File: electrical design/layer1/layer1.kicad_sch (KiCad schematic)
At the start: 183 parts, among them J1 XT60-F, J2 1x07 2.54 FEMALE, J3 1x07 2.54 FEMALE, Q1 MOSFET-NCH-FQP30N06L, Q2 MOSFET-NCH-AO3404A, SW1 SW_DPDT_x2, U1 CD74HC4067SM, U2 CD74HC4067SM

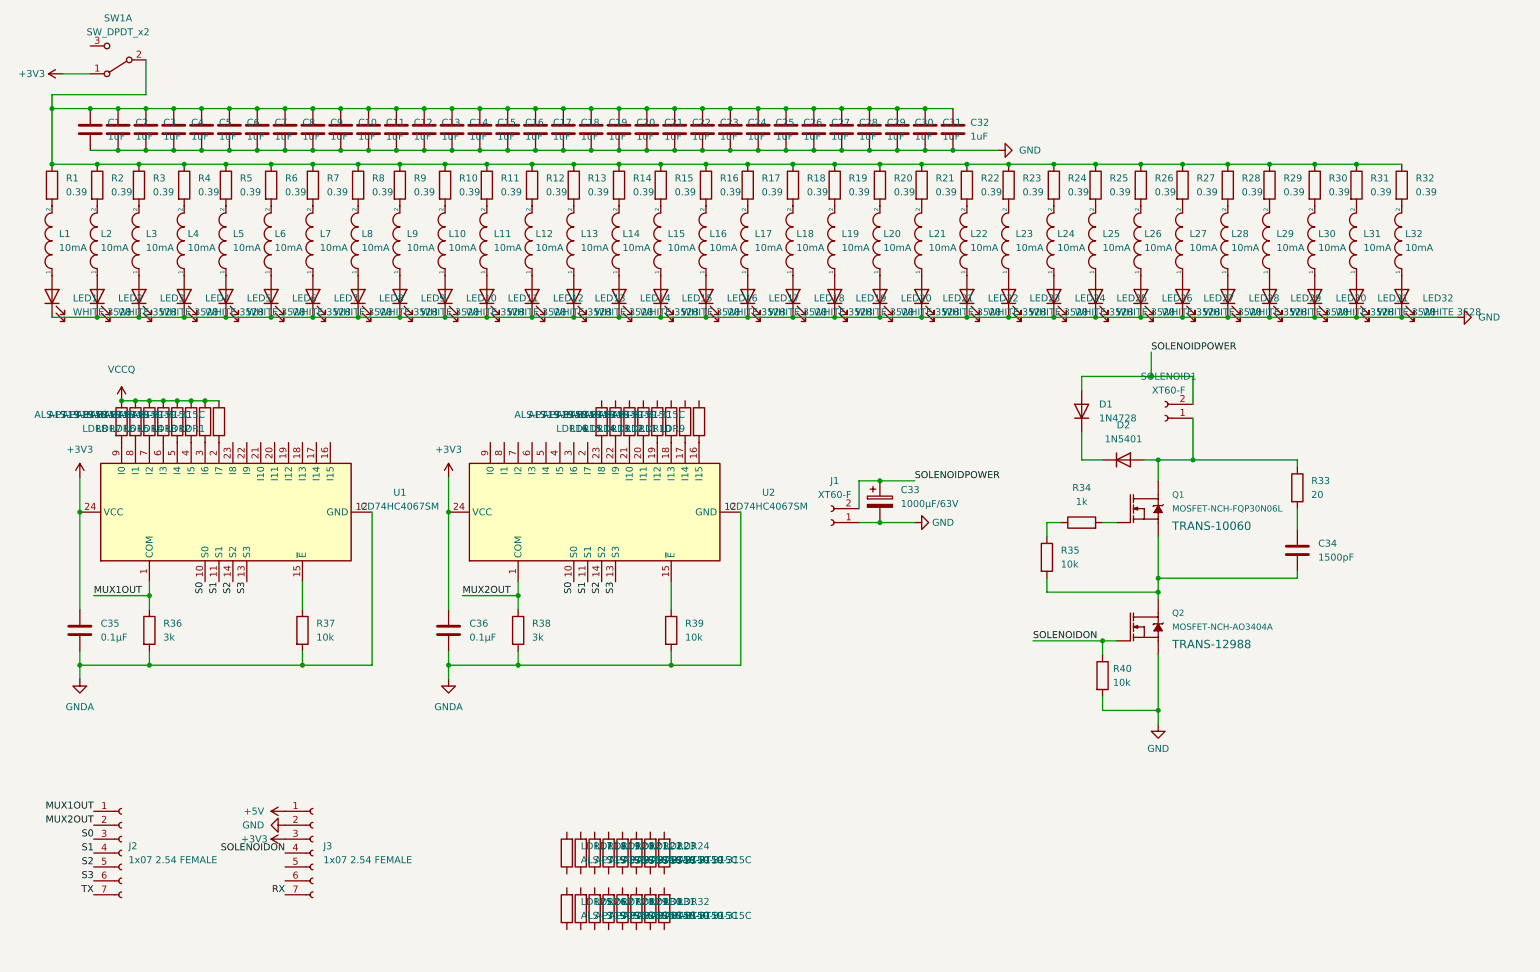
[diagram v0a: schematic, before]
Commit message: update layer 1 pcb
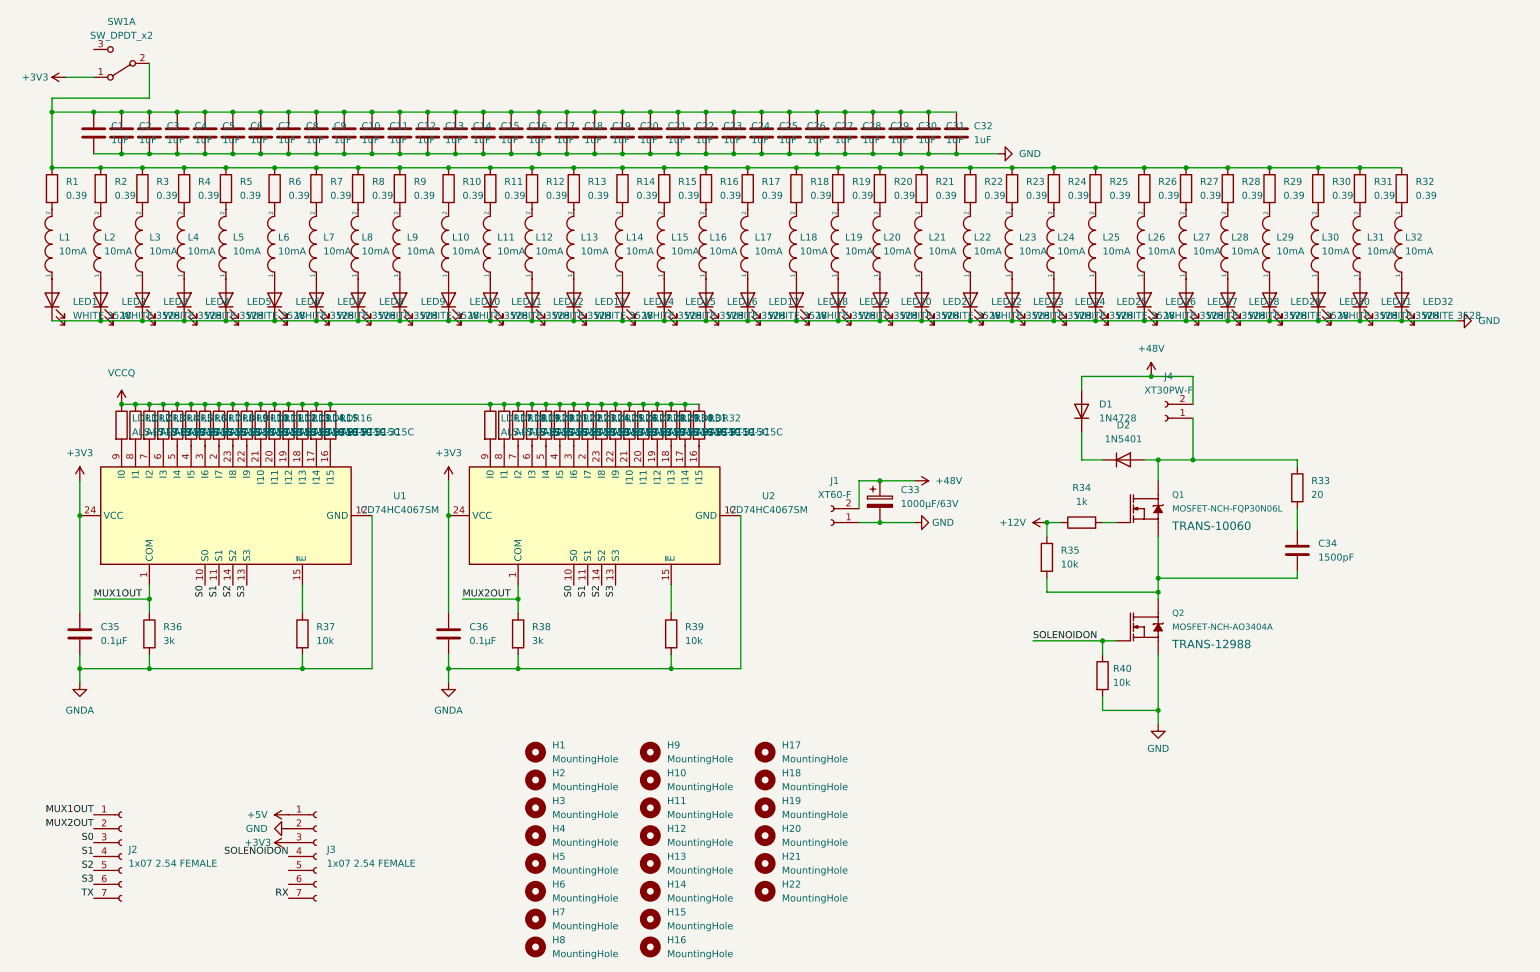
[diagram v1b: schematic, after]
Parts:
- added H1, H10, H11, H12, H13, H14, H15, H16, H17, H18, H19, H2, H20, H21, H22, H3, H4, H5, H6, H7, H8, H9: MountingHole, MountingHole:MountingHole_3.2mm_M3_Pad, symbol Mechanical:MountingHole
- J4: renamed from SOLENOID1; value XT60-F -> XT30PW-F; footprint Connector_AMASS:AMASS_XT30UPB-F_1x02_P5.0mm_Vertical -> Connector_AMASS:AMASS_XT30PW-F_1x02_P2.50mm_Horizontal
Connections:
- net VCCQ: now also LDR10.1, LDR11.1, LDR12.1, LDR13.1, LDR14.1, LDR15.1, LDR16.1, LDR17.1, LDR18.1, LDR19.1, LDR20.1, LDR21.1, LDR22.1, LDR23.1, LDR24.1, LDR25.1, LDR26.1, LDR27.1, LDR28.1, LDR29.1, LDR30.1, LDR31.1, LDR32.1, LDR9.1
- net at U1.16 (I15): now also LDR16.2
- net at U1.17 (I14): now also LDR15.2
- net at U1.18 (I13): now also LDR14.2
- net at U1.19 (I12): now also LDR13.2
- net at U1.2 (I7): now also LDR8.2; no longer LDR1.2
- net at U1.20 (I11): now also LDR12.2
- net at U1.21 (I10): now also LDR11.2
- net at U1.22 (I9): now also LDR10.2
- net at U1.23 (I8): now also LDR9.2
- net at U1.3 (I6): now also LDR7.2; no longer LDR2.2
- net at U1.4 (I5): now also LDR6.2; no longer LDR3.2
- net at U1.5 (I4): now also LDR5.2; no longer LDR4.2
- net at U1.6 (I3): now also LDR4.2; no longer LDR5.2
- net at U1.7 (I2): now also LDR3.2; no longer LDR6.2
- net at U1.8 (I1): now also LDR2.2; no longer LDR7.2
- net at U1.9 (I0): now also LDR1.2; no longer LDR8.2
- net +12V: now reaches R34.1, R35.1
- net at LDR28.2: now also U2.20 (I11)
- net at U2.16 (I15): now also LDR32.2; no longer LDR9.2
- net at U2.17 (I14): now also LDR31.2; no longer LDR10.2
- net at U2.18 (I13): now also LDR30.2; no longer LDR11.2
- net at U2.19 (I12): now also LDR29.2; no longer LDR12.2
- net at U2.2 (I7): now also LDR24.2
- net at U2.21 (I10): now also LDR27.2; no longer LDR14.2
- net at U2.22 (I9): now also LDR26.2; no longer LDR15.2
- net at U2.23 (I8): now also LDR25.2; no longer LDR16.2
- net at U2.3 (I6): now also LDR23.2
- net at U2.4 (I5): now also LDR22.2
- net at U2.5 (I4): now also LDR21.2
- net at U2.6 (I3): now also LDR20.2
- net at U2.7 (I2): now also LDR19.2
- net at U2.8 (I1): now also LDR18.2
- net at U2.9 (I0): now also LDR17.2
- net SOLENOIDPOWER renamed +48V
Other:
- company: (none) -> 8076ducc Robotics Competition Team
- title: (none) -> layer 1 schematic drawing
- moved on the sheet: C1, C10, C11, C12, C13, C14, C15, C16, C17, C18, C19, C2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

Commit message: add boost to l1 pcb and update mech drawing
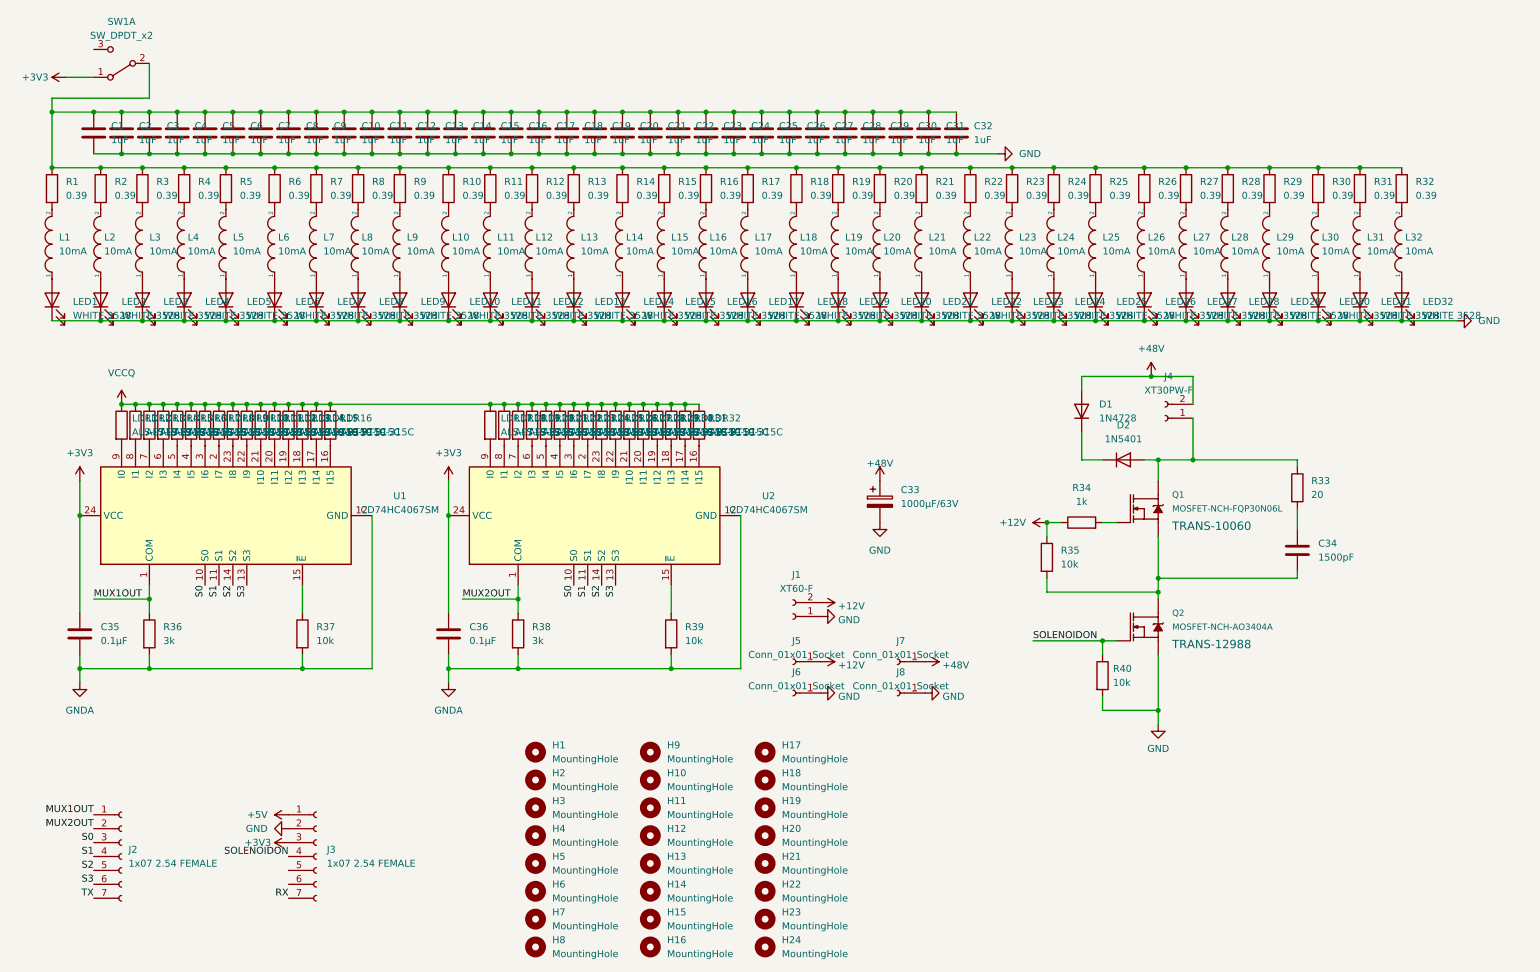
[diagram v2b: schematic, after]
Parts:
- added H23, H24: MountingHole, MountingHole:MountingHole_3.2mm_M3_Pad, symbol Mechanical:MountingHole
- added J5, J6, J7, J8: Conn_01x01_Socket, Connector_Wire:SolderWirePad_1x01_SMD_5x10mm, symbol Connector:Conn_01x01_Socket
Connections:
- net +12V: now also J1.2 (Pin_2), J5.1 (Pin_1)
- net +48V: now also J7.1 (Pin_1); no longer J1.2 (Pin_2)
- net GND: now also J6.1 (Pin_1), J8.1 (Pin_1)
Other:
- moved on the sheet: J1

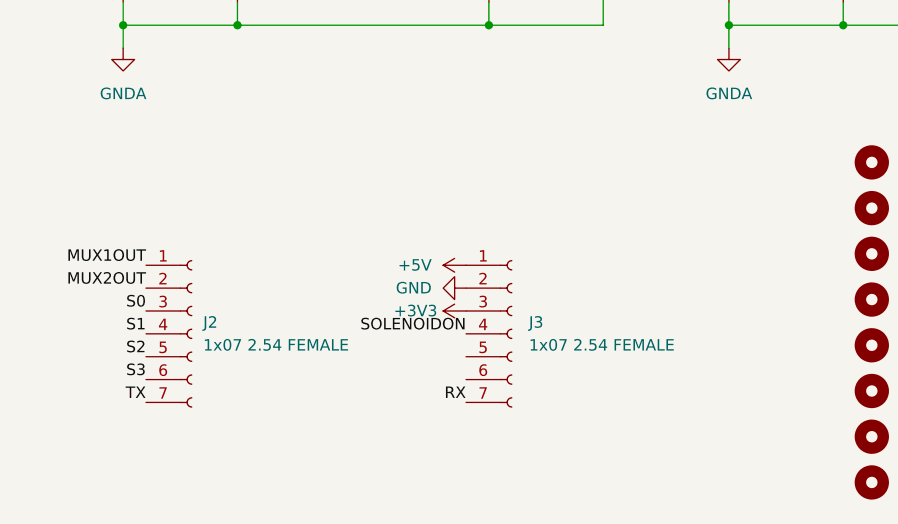
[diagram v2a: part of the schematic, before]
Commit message: route l1 signal lines and resolve drc issues
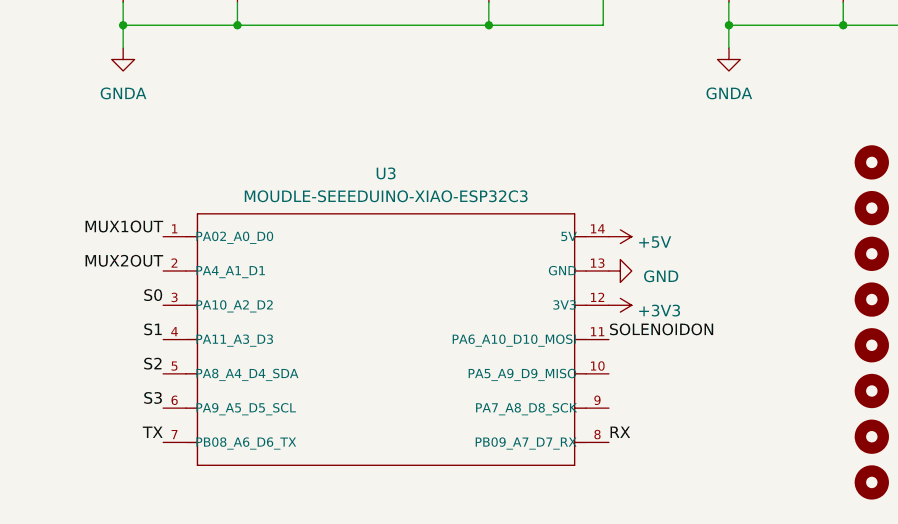
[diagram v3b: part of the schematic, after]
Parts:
- removed J2, J3: 1x07 2.54 FEMALE, Connector_PinHeader_2.54mm:PinHeader_1x07_P2.54mm_Vertical, symbol Connector:Conn_01x07_Female
- added U3: MOUDLE-SEEEDUINO-XIAO-ESP32C3, libraries:xiao-esp32c3, symbol MOUDLE-SEEEDUINO-XIAO-ESP32C3:MOUDLE-SEEEDUINO-XIAO-ESP32C3
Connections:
- net +3V3: now also U3.12 (3V3)
- net +5V: now also U3.14 (5V)
- net GND: now also U3.13 (GND)
- net MUX1OUT: now also U3.1 (PA02_A0_D0)
- net MUX2OUT: now also U3.2 (PA4_A1_D1)
- net RX: now also U3.8 (PB09_A7_D7_RX)
- net S0: now also U3.3 (PA10_A2_D2)
- net S1: now also U3.4 (PA11_A3_D3)
- net S2: now also U3.5 (PA8_A4_D4_SDA)
- net S3: now also U3.6 (PA9_A5_D5_SCL)
- net SOLENOIDON: now also U3.11 (PA6_A10_D10_MOSI)
- net TX: now also U3.7 (PB08_A6_D6_TX)
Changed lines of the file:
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@@
     (stroke (width 0) (type default))
   )
-  (label "MUX1OUT" (at 29.21 163.83 180) (fields_autoplaced)
+  (label "MUX1OUT" (at 31.115 160.655 180) (fields_autoplaced)
     (effects (font (size 1.27 1.27)) (justify right bottom))
   )
@@
     (effects (font (size 1.27 1.27)) (justify right bottom))
   )
-  (label "MUX2OUT" (at 29.21 166.37 180) (fields_autoplaced)
+  (label "MUX2OUT" (at 31.115 164.465 180) (fields_autoplaced)
     (effects (font (size 1.27 1.27)) (justify right bottom))
   )
-  (label "S3" (at 29.21 176.53 180) (fields_autoplaced)
+  (label "S3" (at 31.115 179.705 180) (fields_autoplaced)
     (effects (font (size 1.27 1.27)) (justify right bottom))
   )
-  (label "S0" (at 29.21 168.91 180) (fields_autoplaced)
+  (label "S0" (at 31.115 168.275 180) (fields_autoplaced)
     (effects (font (size 1.27 1.27)) (justify right bottom))
   )
@@
     (effects (font (size 1.27 1.27)) (justify right bottom))
   )
-  (label "RX" (at 64.77 179.07 180) (fields_autoplaced)
-    (effects (font (size 1.27 1.27)) (justify right bottom))
+  (label "RX" (at 80.645 183.515 0) (fields_autoplaced)
+    (effects (font (size 1.27 1.27)) (justify left bottom))
   )
   (label "MUX1OUT" (at 29.21 124.46 0) (fields_autoplaced)
     (effects (font (size 1.27 1.27)) (justify left bottom))
   )
-  (label "S2" (at 29.21 173.99 180) (fields_autoplaced)
+  (label "S2" (at 31.115 175.895 180) (fields_autoplaced)
     (effects (font (size 1.27 1.27)) (justify right bottom))
   )
@@
     (effects (font (size 1.27 1.27)) (justify right bottom))
   )
-  (label "S1" (at 29.21 171.45 180) (fields_autoplaced)
+  (label "S1" (at 31.115 172.085 180) (fields_autoplaced)
     (effects (font (size 1.27 1.27)) (justify right bottom))
   )
-  (label "TX" (at 29.21 179.07 180) (fields_autoplaced)
+  (label "TX" (at 31.115 183.515 180) (fields_autoplaced)
     (effects (font (size 1.27 1.27)) (justify right bottom))
   )
-  (label "SOLENOIDON" (at 64.77 171.45 180) (fields_autoplaced)
-    (effects (font (size 1.27 1.27)) (justify right bottom))
+  (label "SOLENOIDON" (at 80.645 172.085 0) (fields_autoplaced)
+    (effects (font (size 1.27 1.27)) (justify left bottom))
   )
   (label "S2" (at 121.92 121.92 270) (fields_autoplaced)
@@
     )
   )
-  (symbol (lib_id "power:GND") (at 64.77 166.37 270) (unit 1)
+  (symbol (lib_id "power:GND") (at 80.645 164.465 90) (unit 1)
     (in_bom yes) (on_board yes) (dnp no) (fields_autoplaced)
-    (property "Reference" "#PWR010" (at 58.42 166.37 0)
+    (property "Reference" "#PWR010" (at 86.995 164.465 0)
       (effects (font (size 1.27 1.27)) hide)
     )
-    (property "Value" "GND" (at 60.96 166.3699 90)
+    (property "Value" "GND" (at 84.455 165.1 90)
       (effects (font (size 1.27 1.27)) (justify right))
     )
-    (property "Footprint" "" (at 64.77 166.37 0)
+    (property "Footprint" "" (at 80.645 164.465 0)
       (effects (font (size 1.27 1.27)) hide)
     )
-    (property "Datasheet" "" (at 64.77 166.37 0)
+    (property "Datasheet" "" (at 80.645 164.465 0)
       (effects (font (size 1.27 1.27)) hide)
     )
@@
     )
   )
-  (symbol (lib_id "power:+5V") (at 64.77 163.83 90) (unit 1)
+  (symbol (lib_id "power:+5V") (at 80.645 160.655 270) (unit 1)
     (in_bom yes) (on_board yes) (dnp no) (fields_autoplaced)
-    (property "Reference" "#PWR09" (at 68.58 163.83 0)
+    (property "Reference" "#PWR09" (at 76.835 160.655 0)
       (effects (font (size 1.27 1.27)) hide)
     )
-    (property "Value" "+5V" (at 60.96 163.8301 90)
+    (property "Value" "+5V" (at 83.82 161.29 90)
       (effects (font (size 1.27 1.27)) (justify left))
     )
-    (property "Footprint" "" (at 64.77 163.83 0)
+    (property "Footprint" "" (at 80.645 160.655 0)
       (effects (font (size 1.27 1.27)) hide)
     )
-    (property "Datasheet" "" (at 64.77 163.83 0)
+    (property "Datasheet" "" (at 80.645 160.655 0)
       (effects (font (size 1.27 1.27)) hide)
     )
@@
     )
   )
-  (symbol (lib_id "power:+3V3") (at 64.77 168.91 90) (unit 1)
+  (symbol (lib_id "power:+3V3") (at 80.645 168.275 270) (unit 1)
     (in_bom yes) (on_board yes) (dnp no) (fields_autoplaced)
-    (property "Reference" "#PWR011" (at 68.58 168.91 0)
+    (property "Reference" "#PWR011" (at 76.835 168.275 0)
       (effects (font (size 1.27 1.27)) hide)
     )
-    (property "Value" "+3V3" (at 61.595 168.9099 90)
+    (property "Value" "+3V3" (at 83.82 168.91 90)
       (effects (font (size 1.27 1.27)) (justify left))
     )
-    (property "Footprint" "" (at 64.77 168.91 0)
+    (property "Footprint" "" (at 80.645 168.275 0)
       (effects (font (size 1.27 1.27)) hide)
     )
-    (property "Datasheet" "" (at 64.77 168.91 0)
+    (property "Datasheet" "" (at 80.645 168.275 0)
       (effects (font (size 1.27 1.27)) hide)
     )
@@
     )
   )
-  (symbol (lib_id "Connector:Conn_01x07_Female") (at 34.29 171.45 0) (unit 1)
-    (in_bom yes) (on_board yes) (dnp no) (fields_autoplaced)
-    (property "Reference" "J2" (at 35.56 170.1799 0)
-      (effects (font (size 1.27 1.27)) (justify left))
-    )
-    (property "Value" "1x07 2.54 FEMALE" (at 35.56 172.7199 0)
-      (effects (font (size 1.27 1.27)) (justify left))
-    )
-    (property "Footprint" "Connector_PinHeader_2.54mm:PinHeader_1x07_P2.54mm_Vertical" (at 34.29 171.45 0)
-      (effects (font (size 1.27 1.27)) hide)
-    )
-    (property "Datasheet" "~" (at 34.29 171.45 0)
-      (effects (font (size 1.27 1.27)) hide)
-    )
-    (pin "1")
-    (pin "2")
-    (pin "3")
-    (pin "4")
-    (pin "5")
-    (pin "6")
-    (pin "7")
-    (instances
-      (project "layer1"
-        (path "/32d54464-fd6f-441d-9cef-d3e4fabf9fe1"
-          (reference "J2") (unit 1)
-        )
-      )
-    )
-  )
   (symbol (lib_id "pspice:INDUCTOR") (at 243.84 59.69 90) (unit 1)
     (in_bom yes) (on_board yes) (dnp no) (fields_autoplaced)
@@
     )
   )
-  (symbol (lib_id "Connector:Conn_01x07_Female") (at 69.85 171.45 0) (unit 1)
-    (in_bom yes) (on_board yes) (dnp no) (fields_autoplaced)
-    (property "Reference" "J3" (at 71.755 170.1799 0)
-      (effects (font (size 1.27 1.27)) (justify left))
-    )
-    (property "Value" "1x07 2.54 FEMALE" (at 71.755 172.7199 0)
-      (effects (font (size 1.27 1.27)) (justify left))
-    )
-    (property "Footprint" "Connector_PinHeader_2.54mm:PinHeader_1x07_P2.54mm_Vertical" (at 69.85 171.45 0)
-      (effects (font (size 1.27 1.27)) hide)
-    )
-    (property "Datasheet" "~" (at 69.85 171.45 0)
-      (effects (font (size 1.27 1.27)) hide)
-    )
-    (pin "1")
-    (pin "2")
-    (pin "3")
-    (pin "4")
-    (pin "5")
-    (pin "6")
-    (pin "7")
-    (instances
-      (project "layer1"
-        (path "/32d54464-fd6f-441d-9cef-d3e4fabf9fe1"
-          (reference "J3") (unit 1)
-        )
-      )
-    )
-  )
   (symbol (lib_id "Device:LED") (at 21.59 69.85 90) (unit 1)
     (in_bom yes) (on_board yes) (dnp no) (fields_autoplaced)
@@
         )
       )
+    )
+  )
+  (symbol (lib_id "MOUDLE-SEEEDUINO-XIAO-ESP32C3:MOUDLE-SEEEDUINO-XIAO-ESP32C3") (at 56.515 172.085 0) (unit 1)
+    (in_bom yes) (on_board yes) (dnp no) (fields_autoplaced)
+    (property "Reference" "U3" (at 55.88 153.67 0)
+      (effects (font (size 1.27 1.27)))
+    )
+    (property "Value" "MOUDLE-SEEEDUINO-XIAO-ESP32C3" (at 55.88 156.21 0)
+      (effects (font (size 1.27 1.27)))
+    )
+    (property "Footprint" "libraries:xiao-esp32c3" (at 56.515 172.085 0)
+      (effects (font (size 1.27 1.27)) (justify bottom) hide)
+    )
+    (property "Datasheet" "" (at 56.515 172.085 0)
+      (effects (font (size 1.27 1.27)) hide)
+    )
+    (pin "1")
+    (pin "10")
+    (pin "11")
+    (pin "12")
+    (pin "13")
+    (pin "14")
+    (pin "2")
+    (pin "3")
+    (pin "4")
+    (pin "5")
+    (pin "6")
+    (pin "7")
+    (pin "8")
+    (pin "9")
+    (instances
+      (project "layer1"
+        (path "/32d54464-fd6f-441d-9cef-d3e4fabf9fe1"
+          (reference "U3") (unit 1)
+        )
+      )
